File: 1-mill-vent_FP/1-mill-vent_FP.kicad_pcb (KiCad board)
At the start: 2 copper layers, 71.1 x 30.5 mm, 16 parts, among them J1 Front_panel_control, SW1 Fan_Down, SW2 Fan_Up, SW3 Power_On, SW4 Power_off

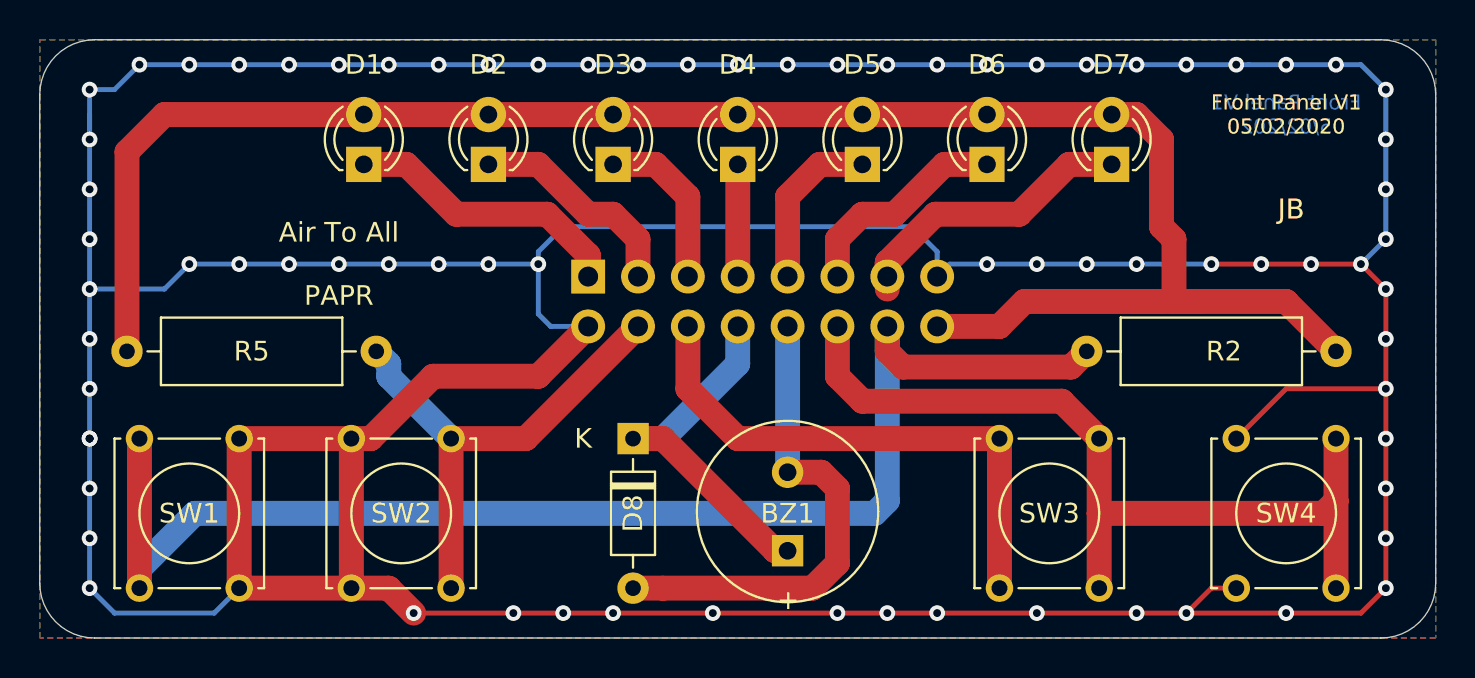
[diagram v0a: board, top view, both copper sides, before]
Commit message: Last update to ver1, start v2
V1 is first board
V2 is start of SMD design
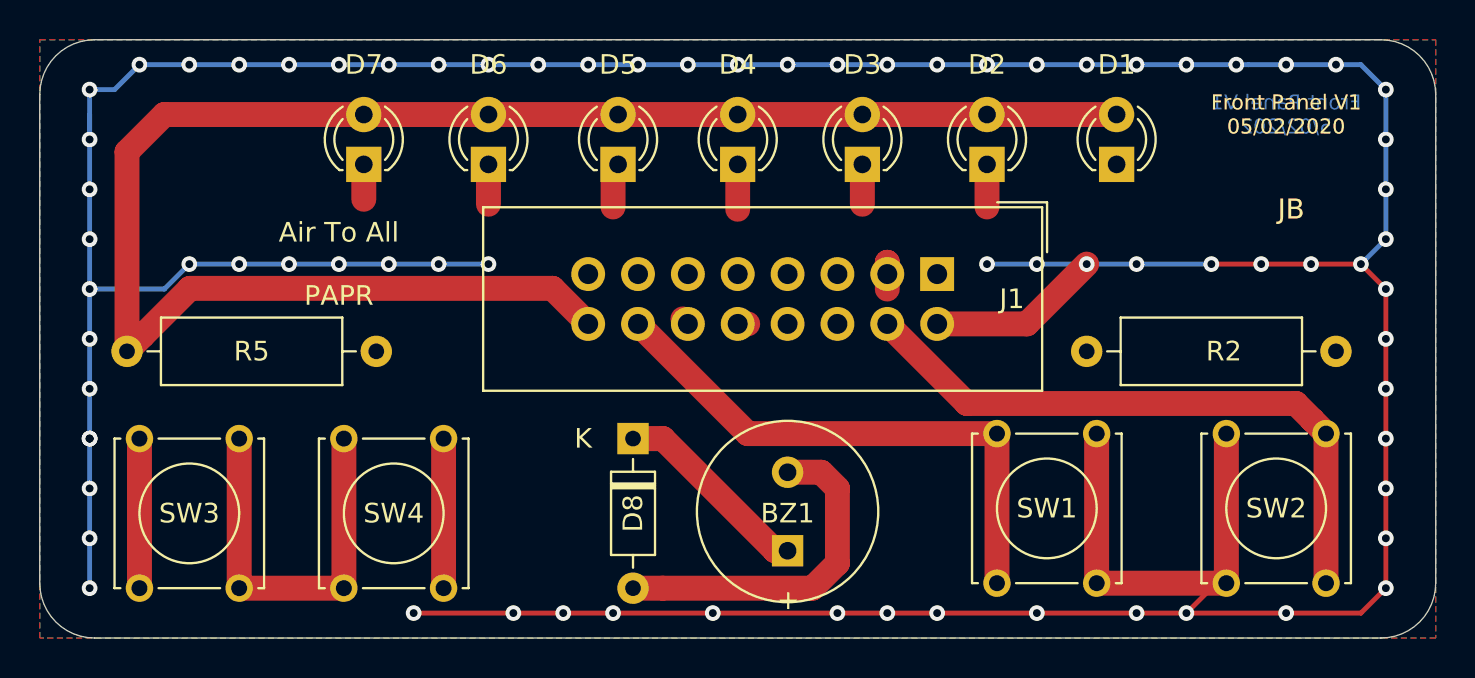
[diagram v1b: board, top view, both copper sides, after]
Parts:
- J1: moved to F.Cu
- moved SW2 44.6 mm to (224.3, 78.5)
- moved SW3 43.8 mm to (174.0, 71.1)
- moved SW1 43.7 mm to (217.7, 70.9)
- moved SW4 41.1 mm to (184.4, 71.1), turned to 270 degrees
- moved D1 38.4 mm to (218.7, 57.1)
- moved D7 38.1 mm to (180.3, 57.1)
- moved D2 25.4 mm to (212.1, 57.1)
- moved D6 25.4 mm to (186.7, 57.1)
- moved J1 17.8 mm to (209.6, 62.7)
- moved D3 12.7 mm to (205.7, 57.1)
- moved D5 12.4 mm to (193.3, 57.1)
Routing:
- net GND: track 310.6 -> 252.8 mm, vias 76 -> 75
- net Down: track 69.1 -> 28.2 mm
- net ON\*OFF: track 44.8 -> 20.9 mm
- net ON: track 27.7 -> 7.62 mm
- net LED1: track 14.9 -> 0.90 mm
- net LED7: track 15.6 -> 1.78 mm
- net +5V: track 97.1 -> 86.7 mm
- net LED6: track 11.1 -> 2.03 mm
- net Buzzer+: track 19.1 -> 11.8 mm
- net Buzzer-: track 25.1 -> 18.1 mm
- net LED2: track 11.1 -> 4.26 mm
- net Up: track 25.5 -> 32.3 mm
- net LED3: track 8.56 -> 2.03 mm
- net LED5: track 8.56 -> 2.17 mm
- net LED4: track 5.72 -> 2.29 mm
